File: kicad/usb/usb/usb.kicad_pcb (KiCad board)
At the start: 2 copper layers, 31 x 27 mm, 20 parts, among them J1 USB_C_Receptacle_USB2.0_14P, J2 PH2.0mm 2P, J3 Conn_01x07_Pin, Q1 MMBT3906, SW1 PWR, U1 S-T111B33MC-OGSTFU, U2 MCP73831-2-OT

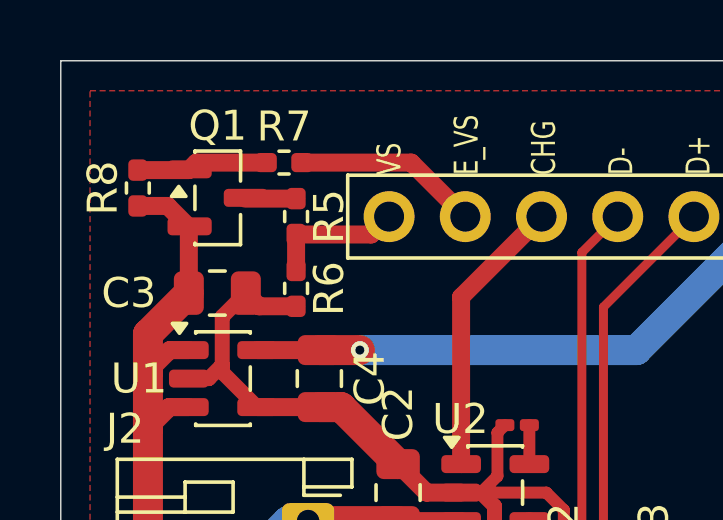
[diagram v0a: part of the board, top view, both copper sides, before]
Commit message: Getting rid of the vdiv switch after some testing
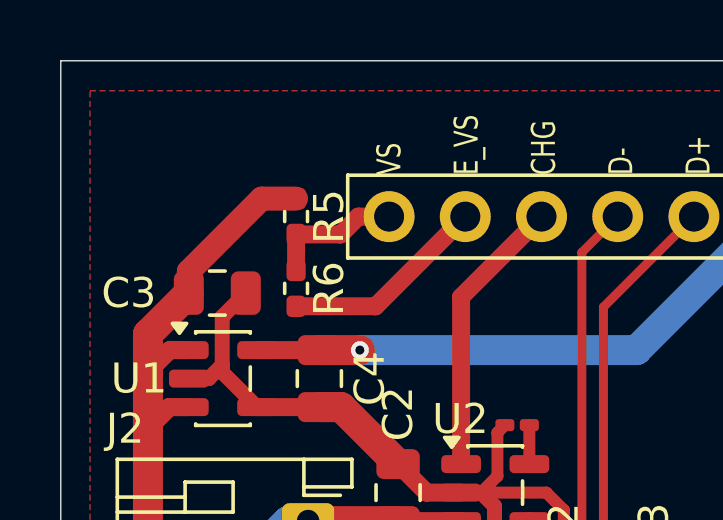
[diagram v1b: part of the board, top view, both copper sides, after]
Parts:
- removed Q1: MMBT3906, Package_TO_SOT_SMD:SOT-23
- removed R7: 100k, Resistor_SMD:R_0402_1005Metric_Pad0.72x0.64mm_HandSolder
- removed R8: 1m, Resistor_SMD:R_0402_1005Metric_Pad0.72x0.64mm_HandSolder
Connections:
- R5 pad 2: Net-(Q1-C) -> VSENSE
- R6 pad 1: GND -> EN_VSENSE
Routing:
- net Net-(Q1-B): track 4.38 -> 0.00 mm
- net GND: track 73.3 -> 71.4 mm
- net Net-(Q1-C): track 1.70 -> 0.00 mm
- net VSENSE: track 26.1 -> 27.2 mm
- net EN_VSENSE: track 6.19 -> 6.88 mm
